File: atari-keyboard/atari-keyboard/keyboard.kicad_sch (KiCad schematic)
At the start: 138 parts, among them SW201 MENU, SW202 TURBO, SW203 RESET, SW204 OPTION, SW205 SELECT, SW206 START, SW207 HELP, SW208 ESC, SW209 RSHIFT, SW210 1, SW211 2, SW212 3, SW213 4, SW214 5, SW215 6, SW216 7, SW217 8, SW218 UP, SW219 9, SW220 0, SW221 <, SW222 >, SW223 BS, SW224 BRK, SW225 TAB, SW226 Q, SW227 DOWN, SW228 W, SW229 E, SW230 R, SW231 T, SW232 Y, SW233 U, SW234 I, SW235 O, SW236 LEFT, SW237 P, SW238 [-], SW239 [=], SW240 RET, SW241 CTRL, SW242 A, SW243 S, SW244 D, SW245 RIGHT, SW246 F, SW247 G, SW248 H, SW249 J, SW250 K, SW251 L, SW252 [;], SW253 [+], SW254 N, SW255 MULT, SW256 CAPS, SW257 LSHIFT, SW258 Z, SW259 X, SW260 C, SW261 V, SW262 B, SW263 M, SW264 FN, SW265 INV, SW266 SPC, SW267 [,], SW268 [.], SW269 [/]

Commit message: Reran placement
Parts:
- SW209: footprint Button_Switch_Keyboard:SW_Cherry_MX_2.00u_PCB -> Button_Switch_Keyboard:SW_Cherry_MX_1.75u_PCB
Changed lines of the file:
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@@
     (property "Reference" "SW209" (id 0) (at 217.805 37.592 0))
     (property "Value" "RSHIFT" (id 1) (at 217.805 39.751 0))
-    (property "Footprint" "Button_Switch_Keyboard:SW_Cherry_MX_2.00u_PCB" (id 2) (at 217.805 43.561 0)
+    (property "Footprint" "Button_Switch_Keyboard:SW_Cherry_MX_1.75u_PCB" (id 2) (at 217.805 43.561 0)
       (effects (font (size 1.27 1.27)) hide)
     )

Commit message: Switched over to hybrid resisters and diodes.
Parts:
- D201, D202, D203, D204, D205, D206, D207, D208, D209, D210, D211, D212, D213, D214, D215, D216, D217, D218, D219, D220, D221, D222, D223, D224, D225, D226, D227, D228, D229, D230, D231, D232, D233, D234, D235, D236, D237, D238, D239, D240, D241, D242, D243, D244, D245, D246, D247, D248, D249, D250, D251, D252, D253, D254, D255, D256, D257, D258, D259, D260, D261, D262, D263, D264, D265, D266, D267, D268, D269: footprint Diode_THT:D_A-405_P7.62mm_Horizontal -> keebio:Diode-dual

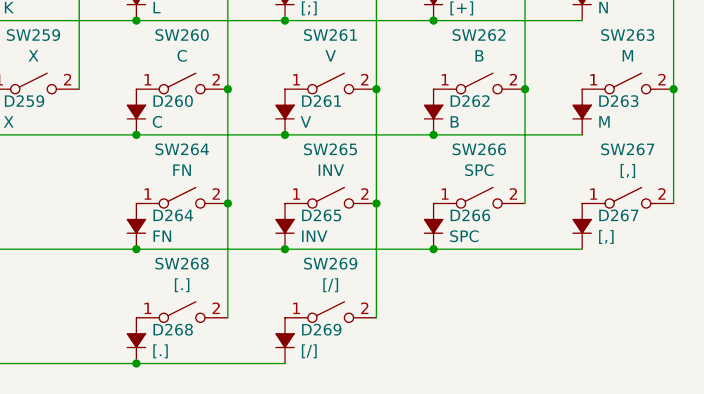
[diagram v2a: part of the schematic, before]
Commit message: Added "POWER" button
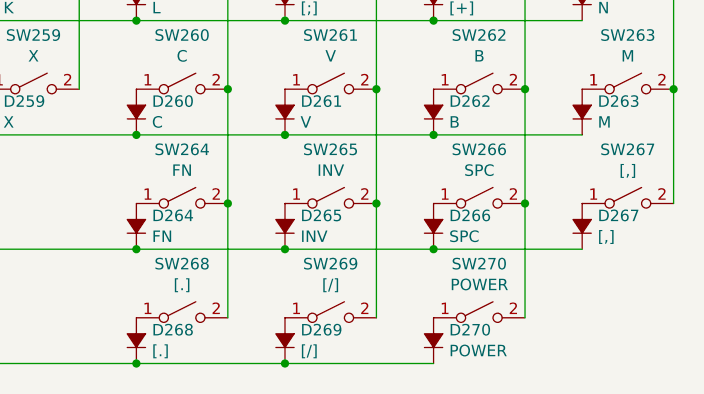
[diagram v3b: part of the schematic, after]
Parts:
- added D270: POWER, keebio:Diode-dual, symbol atari-keyboard-rescue:D_Small_ALT-Device
- added SW270: POWER, Button_Switch_Keyboard:SW_Cherry_MX_1.00u_PCB, symbol Switch:SW_SPST
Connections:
- net C8: now also SW270.2 (B)
- net R9: now also D270.1 (K)
- new net: D270.2 (A), SW270.1 (A)
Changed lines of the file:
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@@
   (junction (at 107.315 94.361) (diameter 0) (color 0 0 0 0)
   )
+  (junction (at 179.705 150.241) (diameter 0) (color 0 0 0 0)
+  )
   (junction (at 163.195 48.641) (diameter 0) (color 0 0 0 0)
   )
@@
   (junction (at 206.375 107.061) (diameter 0) (color 0 0 0 0)
   )
+  (junction (at 206.375 132.461) (diameter 0) (color 0 0 0 0)
+  )
   (junction (at 196.215 99.441) (diameter 0) (color 0 0 0 0)
   )
@@
     (stroke (width 0) (type default) (color 0 0 0 0))
   )
+  (wire (pts (xy 179.705 150.241) (xy 196.215 150.241))
+    (stroke (width 0) (type default) (color 0 0 0 0))
+  )
   (wire (pts (xy 97.155 74.041) (xy 113.665 74.041))
     (stroke (width 0) (type default) (color 0 0 0 0))
@@
   )
   (wire (pts (xy 140.335 43.561) (xy 140.335 56.261))
+    (stroke (width 0) (type default) (color 0 0 0 0))
+  )
+  (wire (pts (xy 206.375 132.461) (xy 206.375 145.161))
     (stroke (width 0) (type default) (color 0 0 0 0))
   )
@@
     (pin "2")
   )
+  (symbol (lib_id "Switch:SW_SPST") (at 201.295 145.161 0) (unit 1)
+    (in_bom yes) (on_board yes)
+    (property "Reference" "SW270" (id 0) (at 201.295 139.192 0))
+    (property "Value" "POWER" (id 1) (at 201.295 141.5034 0))
+    (property "Footprint" "Button_Switch_Keyboard:SW_Cherry_MX_1.00u_PCB" (id 2) (at 201.295 145.161 0)
+      (effects (font (size 1.27 1.27)) hide)
+    )
+    (property "Datasheet" "~" (id 3) (at 201.295 145.161 0)
+      (effects (font (size 1.27 1.27)) hide)
+    )
+    (pin "1")
+    (pin "2")
+  )
   (symbol (lib_id "Switch:SW_SPST") (at 102.235 107.061 0) (unit 1)
     (in_bom yes) (on_board yes)
@@
       (effects (font (size 1.27 1.27)) hide)
     )
+    (pin "1")
+    (pin "2")
+  )
+  (symbol (lib_id "atari-keyboard-rescue:D_Small_ALT-Device") (at 196.215 147.701 90) (unit 1)
+    (in_bom yes) (on_board yes)
+    (property "Reference" "D270" (id 0) (at 197.9422 146.5326 90)
+      (effects (font (size 1.27 1.27)) (justify right))
+    )
+    (property "Value" "POWER" (id 1) (at 197.9422 148.844 90)
+      (effects (font (size 1.27 1.27)) (justify right))
+    )
+    (property "Footprint" "keebio:Diode-dual" (id 2) (at 196.215 147.701 90)
+      (effects (font (size 1.27 1.27)) hide)
+    )
+    (property "Datasheet" "~" (id 3) (at 196.215 147.701 90)
+      (effects (font (size 1.27 1.27)) hide)
+    )

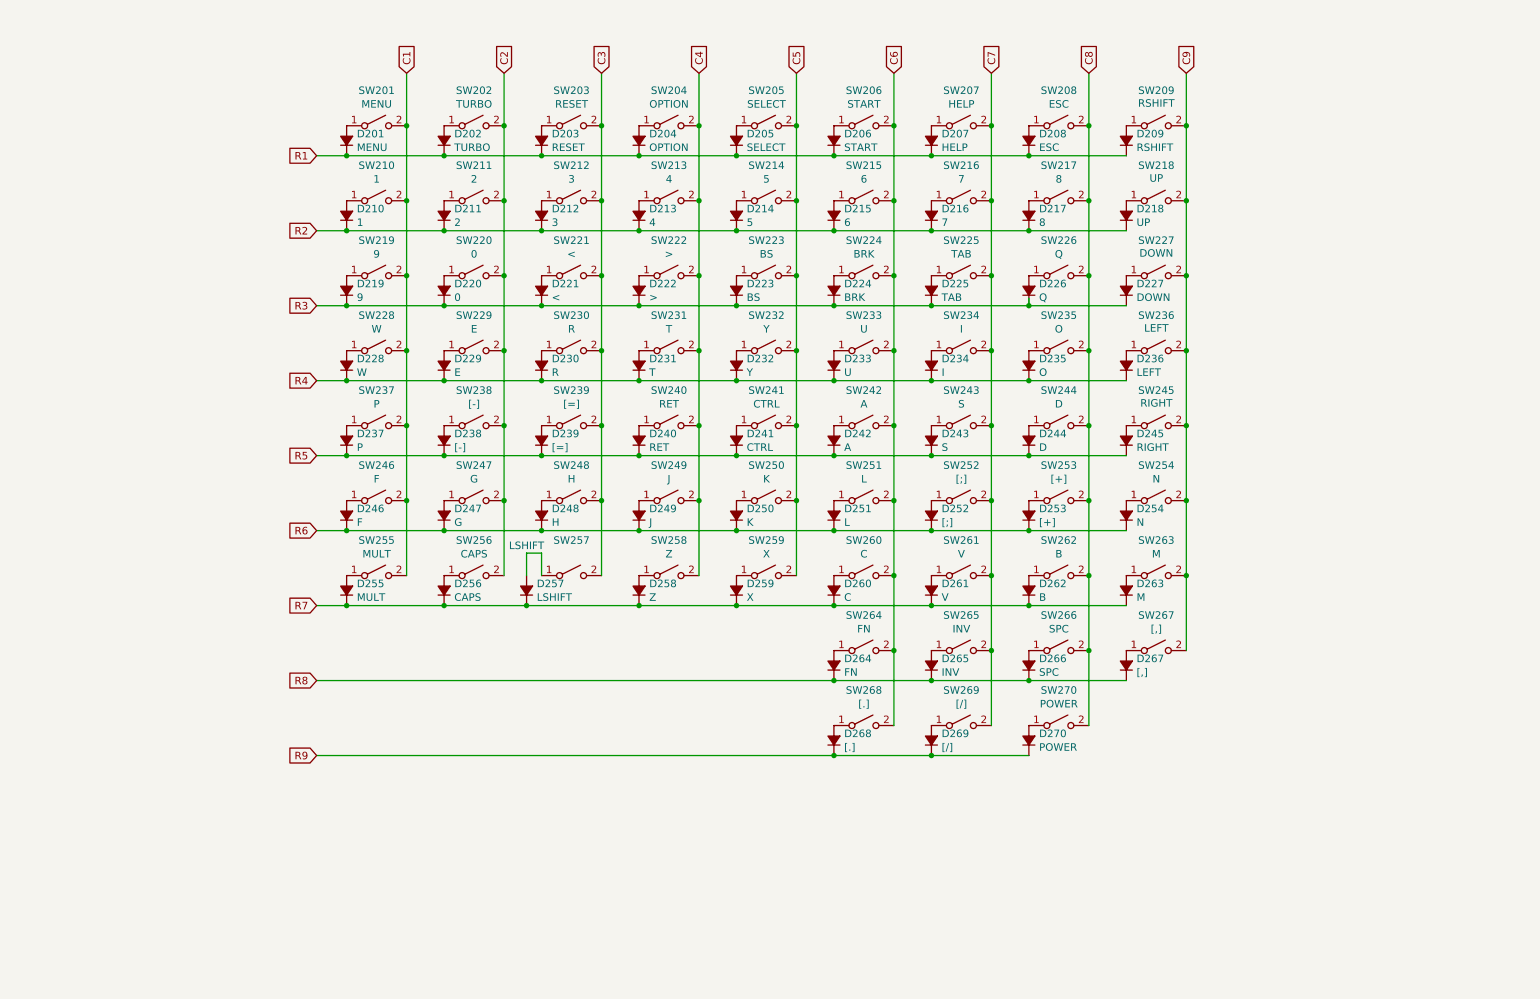
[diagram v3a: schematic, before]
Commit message: Added mounting holes and did part layout.
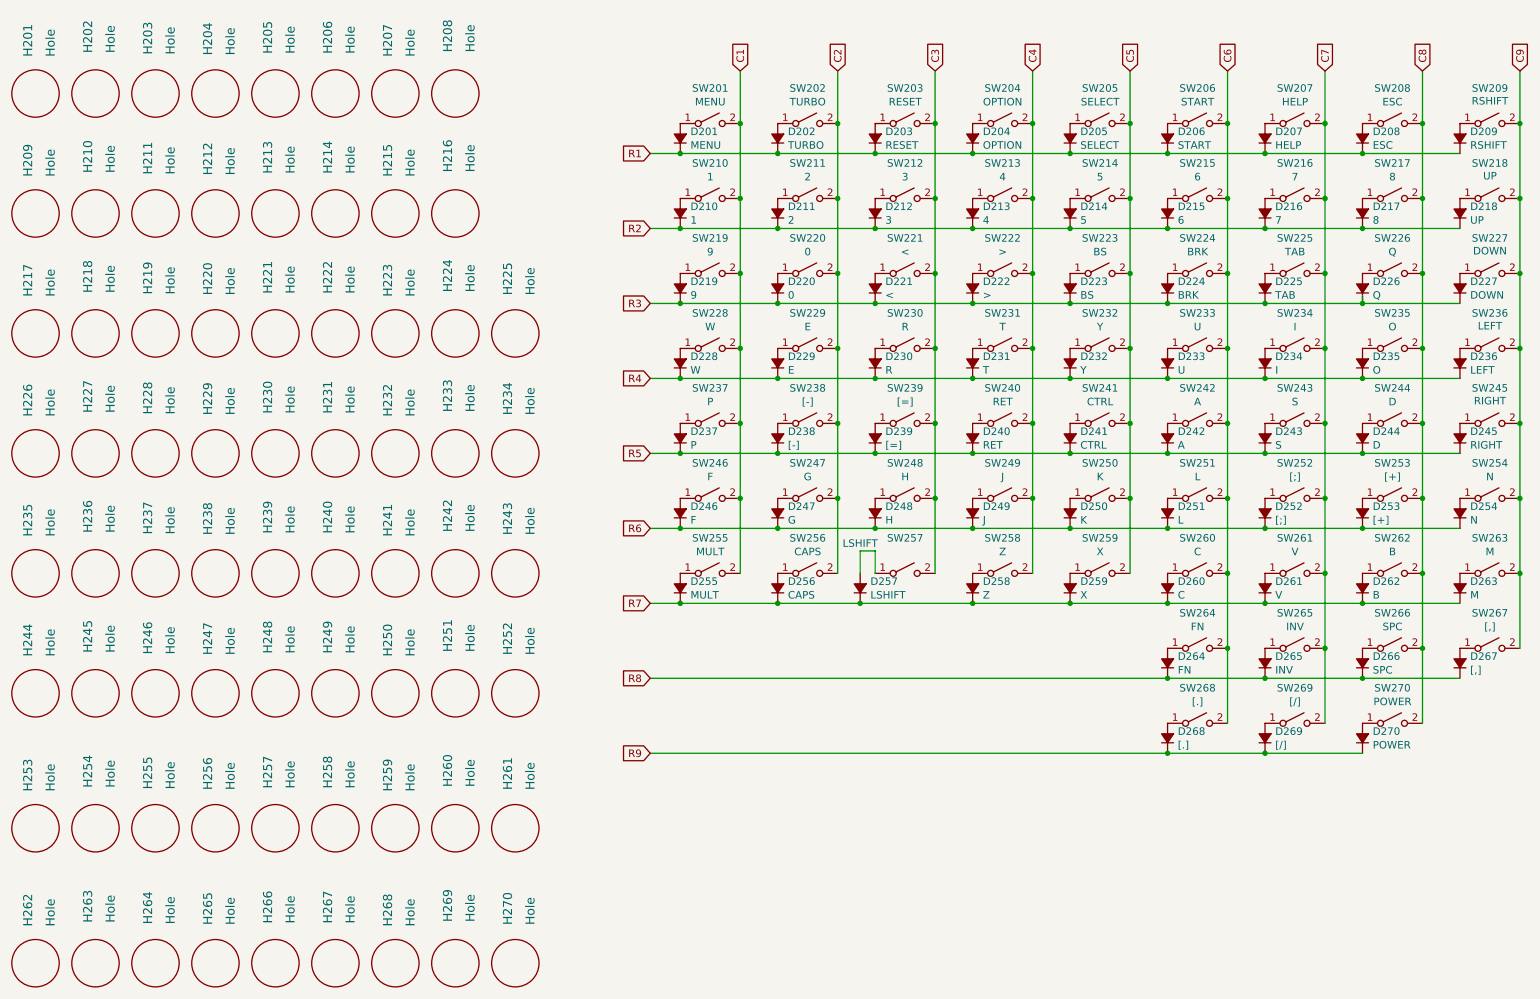
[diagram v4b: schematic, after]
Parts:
- added H201, H202, H203, H204, H205, H206, H207, H208, H209, H210, H211, H212, H213, H214, H215, H216, H217, H218, H219, H220, H221, H222, H223, H224, H225, H226, H227, H228, H229, H230, H231, H232, H233, H234, H235, H236, H237, H238, H239, H240, H241, H242, H243, H244, H245, H246, H247, H248, H249, H250, H251, H252, H253, H254, H255, H256, H257, H258, H259, H260, H261, H262, H263, H264, H265, H266, H267, H268, H269, H270: Hole, MountingHole:MountingHole_2.2mm_M2, symbol keebio:Hole
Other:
- moved on the sheet: D201, D202, D203, D204, D205, D206, D207, D208, D209, D210, D211, D212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

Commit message: mounting holes in place
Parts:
- D201, D202, D203, D204, D205, D206, D207, D208, D209, D210, D211, D212, D213, D214, D215, D216, D217, D218, D219, D220, D221, D222, D223, D224, D225, D226, D227, D228, D229, D230, D231, D232, D233, D234, D235, D236, D237, D238, D239, D240, D241, D242, D243, D244, D245, D246, D247, D248, D249, D250, D251, D252, D253, D254, D255, D256, D257, D258, D259, D260, D261, D262, D263, D264, D265, D266, D267, D268, D269, D270: footprint keebio:Diode-dual -> retro-kbd:Diode-dual

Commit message: Added a software switch between fdm and resin printing and cleaned up row issue.
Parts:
- H201: JJSJJS (none) -> JOY_HOPE
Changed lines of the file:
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@@
       (effects (font (size 1.524 1.524)) hide)
+    )
+    (property "JJSJJS" "JOY_HOPE" (id 4) (at 27.94 38.1 0)
+      (effects (font (size 1.27 1.27)) hide)
     )
   )

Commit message: Added the keyboard mounting hole offsets.
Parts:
- H201: JJSJJS JOY_HOPE -> MINE
- H240: PCB_X (none) -> 2; PCB_Y (none) -> 7
- H257: PCB_Y (none) -> 7
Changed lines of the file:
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@@
       (effects (font (size 1.524 1.524)) hide)
+    )
+    (property "PCB_Y" "7" (id 4) (at 68.58 162.56 0)
+      (effects (font (size 1.27 1.27)) hide)
     )
   )
@@
       (effects (font (size 1.524 1.524)) hide)
     )
-    (property "JJSJJS" "JOY_HOPE" (id 4) (at 27.94 38.1 0)
+    (property "JJSJJS" "MINE" (id 4) (at 27.94 38.1 0)
       (effects (font (size 1.27 1.27)) hide)
     )
@@
       (effects (font (size 1.524 1.524)) hide)
     )
-  )
+    (property "PCB_X" "2" (id 4) (at 78.74 119.38 0)
+      (effects (font (size 1.27 1.27)) hide)
+    )
+    (property "PCB_Y" "7" (id 5) (at 78.74 119.38 0)
+      (effects (font (size 1.27 1.27)) hide)
+    )
+  )
